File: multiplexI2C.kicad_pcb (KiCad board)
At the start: 2 copper layers, 48.3 x 71.1 mm, 58 parts, among them J1 Screw_Terminal_01x04, J10 Screw_Terminal_01x02, J2 Screw_Terminal_01x04, J3 Screw_Terminal_01x04, J4 Screw_Terminal_01x04, J5 Screw_Terminal_01x04, J6 Screw_Terminal_01x04, J7 Screw_Terminal_01x04, J8 Screw_Terminal_01x04, J9 Conn_02x04_Top_Bottom, U1 PCA9548A, U2 AMS1117-3.3 SOT-223, U3 f411-RFM95W

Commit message: cleaned up fab layer annotation.
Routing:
- net GND: track 69.9 -> 67.0 mm
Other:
- board text removed: "ADS1115IDGS"
- board text removed: "BT1"
- board text removed: "Battery_Cell_Holder"
- board text removed: "H1"
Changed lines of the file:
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@@
 		)
 		(property "Value" "1µF"
-			(at 1.33 0.19 90)
+			(at 2.9 0.22 90)
 			(layer "F.Fab")
 			(effects
@@
 		)
 		(property "Value" "MountingHole"
-			(at 1.34 4.23 0)
+			(at -3.76 6.2 45)
 			(layer "F.Fab")
 			(effects
@@
 		)
 		(property "Value" "TestPoint"
-			(at 0 1.55 0)
+			(at 3.87 -2.39 45)
 			(layer "F.Fab")
 			(effects
@@
 		(tags "SOT TO_SOT_SMD")
 		(property "Reference" "D3"
-			(at 0 -2.4 180)
+			(at 0.75 2.31 180)
 			(layer "F.SilkS")
 			(effects
@@
 		)
 		(property "Value" "BAT54C-HF"
-			(at -3.29 0.05 180)
+			(at -4.63 2.54 225)
 			(layer "F.Fab")
 			(effects
@@
 		)
 		(property "Value" "100nF"
-			(at 2.09 -0.09 90)
+			(at 3.25 0 90)
 			(layer "F.Fab")
 			(effects
@@
 		)
 		(property "Value" "Screw_Terminal_01x04"
-			(at 20.25 3.5 0)
+			(at 16.61 -6.03 45)
 			(layer "F.Fab")
 			(effects
@@
 		)
 		(property "Value" "0.1µF"
-			(at 0 1.16 0)
+			(at -0.06 -1.32 0)
 			(layer "F.Fab")
 			(effects
@@
 		)
 		(property "Value" "100nF"
-			(at 2.08 -0.05 90)
+			(at 3.37 0.2 90)
 			(layer "F.Fab")
 			(effects
@@
 		)
 		(property "Value" "MountingHole"
-			(at -7.67 -1.46 0)
+			(at 3.4 -6.43 45)
 			(layer "F.Fab")
 			(effects
@@
 		)
 		(property "Value" "100nF"
-			(at 2.11 -0.06 90)
+			(at 3.33 -0.07 90)
 			(layer "F.Fab")
 			(effects
@@
 		)
 		(property "Value" "MountingHole"
-			(at -1.12 3.57 0)
+			(at -3.27 5.84 45)
 			(layer "F.Fab")
 			(effects
@@
 		)
 		(property "Value" "Screw_Terminal_01x04"
-			(at -8.973 11.9275 0)
+			(at 17.127 -4.8825 45)
 			(layer "F.Fab")
 			(effects
@@
 		)
 		(property "Value" "AMS1117-3.3 SOT-223"
-			(at 0 4.5 0)
+			(at 6.81 -11.2 45)
 			(layer "F.Fab")
 			(effects
@@
 		)
 		(property "Value" "PCA9548A"
-			(at 0 4.85 0)
+			(at -4.5745 1.1075 45)
 			(layer "F.Fab")
 			(effects
@@
 		)
 		(property "Value" "f411-RFM95W"
-			(at -1.45 8.63 0)
+			(at 12.15 0.32 45)
 			(layer "F.Fab")
 			(effects
@@
 		)
 		(property "Value" "Screw_Terminal_01x02"
-			(at 1.016 12.192 90)
+			(at -4.73 10.33 45)
 			(layer "F.Fab")
 			(effects
@@
 		)
 		(property "Value" "100nF"
-			(at 0 0 90)
+			(at -3.3 0.03 90)
 			(layer "F.Fab")
 			(effects
@@
 		)
 		(property "Value" "MountingHole"
-			(at 1.629 -3.049 0)
+			(at 6.3 -5.77 45)
 			(layer "F.Fab")
 			(effects
@@
 		)
 		(property "Value" "0.1µF"
-			(at 0 0 180)
+			(at 0.36 1.21 180)
 			(layer "B.Fab")
 			(effects
@@
 		)
 		(property "Value" "4.7k"
-			(at 0 -0.1 90)
+			(at 2.04 1.4 90)
 			(layer "B.Fab")
 			(effects
@@
 		)
 		(property "Value" "100nF"
-			(at -0.22 -0.1 0)
+			(at -0.49 -1.11 0)
 			(layer "B.Fab")
 			(effects
@@
 		)
 		(property "Value" "0.1µF"
-			(at -0.75 0 0)
+			(at -0.39 1.32 0)
 			(layer "B.Fab")
 			(effects
@@
 			(at 0 7 180)
 			(layer "B.Fab")
+			(hide yes)
 			(effects
 				(font
@@
 		)
 		(property "Package" "BatteryHolder_LINX_BAT-HLD-012-SMT"
-			(at 0 0 180)
+			(at 13.87 7.61 315)
 			(unlocked yes)
 			(layer "B.Fab")
-			(hide yes)
 			(effects
 				(font
@@
 		)
 		(fp_text user "Pad  2 battery contact - no solder paste"
-			(at -0.29 -12.27 0)
+			(at 23.97 25.7 315)
 			(unlocked yes)
 			(layer "B.Fab")
@@
 		)
 		(property "Value" "4.7k"
-			(at -0.2 -0.15 90)
+			(at -0.95 -1.21 90)
 			(layer "B.Fab")
 			(effects
@@
 		)
 		(property "Value" "0.1µF"
-			(at 0 0 180)
+			(at 0.67 1.18 180)
 			(layer "B.Fab")
 			(effects
@@
 		)
 		(property "Value" "0.1µF"
-			(at 0 0 180)
+			(at 0.26 1.11 180)
 			(layer "B.Fab")
 			(effects
@@
 		)
 		(property "Value" "4.7k"
-			(at 0 0.1 90)
+			(at -1.28 -1.27 90)
 			(layer "B.Fab")
 			(effects
@@
 		)
 		(property "Value" "0.1µF"
-			(at 0 0 0)
+			(at 0.5 1.19 0)
 			(layer "B.Fab")
 			(effects
@@
 		)
 		(property "Value" "0.1µF"
-			(at 0 -1.16 0)
+			(at 0.6 1.05 0)
 			(layer "B.Fab")
 			(effects
@@
 		)
 		(property "Value" "0.1µF"
-			(at -0.38 -0.1 180)
+			(at 1.32 1.13 180)
 			(layer "B.Fab")
 			(effects
@@
 		)
 	)
-	(gr_text "Battery_Cell_Holder"
-		(at 87.609998 46.01 90)
-		(layer "B.Fab")
-		(effects
-			(font
-				(size 1 1)
-				(thickness 0.15)
-			)
-			(justify mirror)
-		)
-	)
-	(gr_text "BT1"
-		(at 87.619999 33.72 0)
-		(layer "B.Fab")
-		(effects
-			(font
-				(size 1 1)
-				(thickness 0.15)
-			)
-			(justify mirror)
-		)
-	)
-	(gr_text "ADS1115IDGS"
-		(at 73.84 56.02 90)
-		(layer "F.Fab")
-		(effects
-			(font
-				(size 1 1)
-				(thickness 0.15)
-			)
-		)
-	)
-	(gr_text "H1"
-		(at 96.29 95.15 0)
-		(layer "F.Fab")
-		(effects
-			(font
-				(size 1 1)
-				(thickness 0.15)
-			)
-		)
-	)
 	(gr_text "U2"
 		(at 72.84 57.02 270)
@@
 	)
 	(segment
-		(start 69.885 60.09)
-		(end 69.885 60.585)
-		(width 0.25)
-		(layer "B.Cu")
-		(net 2)
-	)
-	(segment
 		(start 64.94 51.65)
 		(end 64.9 51.69)
@@
 	)
 	(segment
-		(start 58.197 60.0775)
-		(end 58.197 60.617)
-		(width 0.25)
-		(layer "B.Cu")
-		(net 2)
-	)
-	(segment
 		(start 70.242 65.9025)
 		(end 70.917 65.2275)
@@
 	)
 	(segment
-		(start 69.84 40.92)
-		(end 69.84 40.44)
-		(width 0.25)
-		(layer "B.Cu")
-		(net 2)
-	)
-	(segment
 		(start 70.242 67.9075)
 		(end 70.242 65.9025)
@@
 	)
 	(segment
-		(start 58.214 33.415)
-		(end 58.214 33.924)
-		(width 0.25)
-		(layer "B.Cu")
-		(net 2)
-	)
-	(segment
 		(start 58.197 60.617)
 		(end 59.34 61.76)
@@
 	)
 	(segment
-		(start 58.182 67.9075)
-		(end 58.182 67.278)
-		(width 0.25)
-		(layer "B.Cu")
-		(net 2)
-	)
-	(segment
 		(start 65.64 51.65)
 		(end 64.94 51.65)
@@
 	)
 	(segment
-		(start 58.214 40.915)
-		(end 58.214 40.656)
-		(width 0.25)
-		(layer "B.Cu")
-		(net 2)
-	)
-	(segment
 		(start 59.07 32.559)
 		(end 58.214 33.415)
@@
 	)
 	(segment
-		(start 55.633 68.2545)
-		(end 55.633 67.9425)
-		(width 0.25)
-		(layer "F.Cu")
-		(net 38)
-	)
-	(segment
 		(start 51.189 56.520805)
 		(end 51.189 68.8905)
@@
 	)
 	(segment
-		(start 55.633 65.893)
-		(end 55.55 65.81)
-		(width 0.25)
-		(layer "B.Cu")
-		(net 38)
-	)
-	(segment
 		(start 52.646695 55.857805)
 		(end 51.639 56.8655)
@@
 		(width 0.25)
 		(layer "B.Cu")
-		(net 39)
-	)
-	(segment
-		(start 53.093 65.857)
-		(end 53.15 65.8)
-		(width 0.25)
-		(layer "B.Cu")

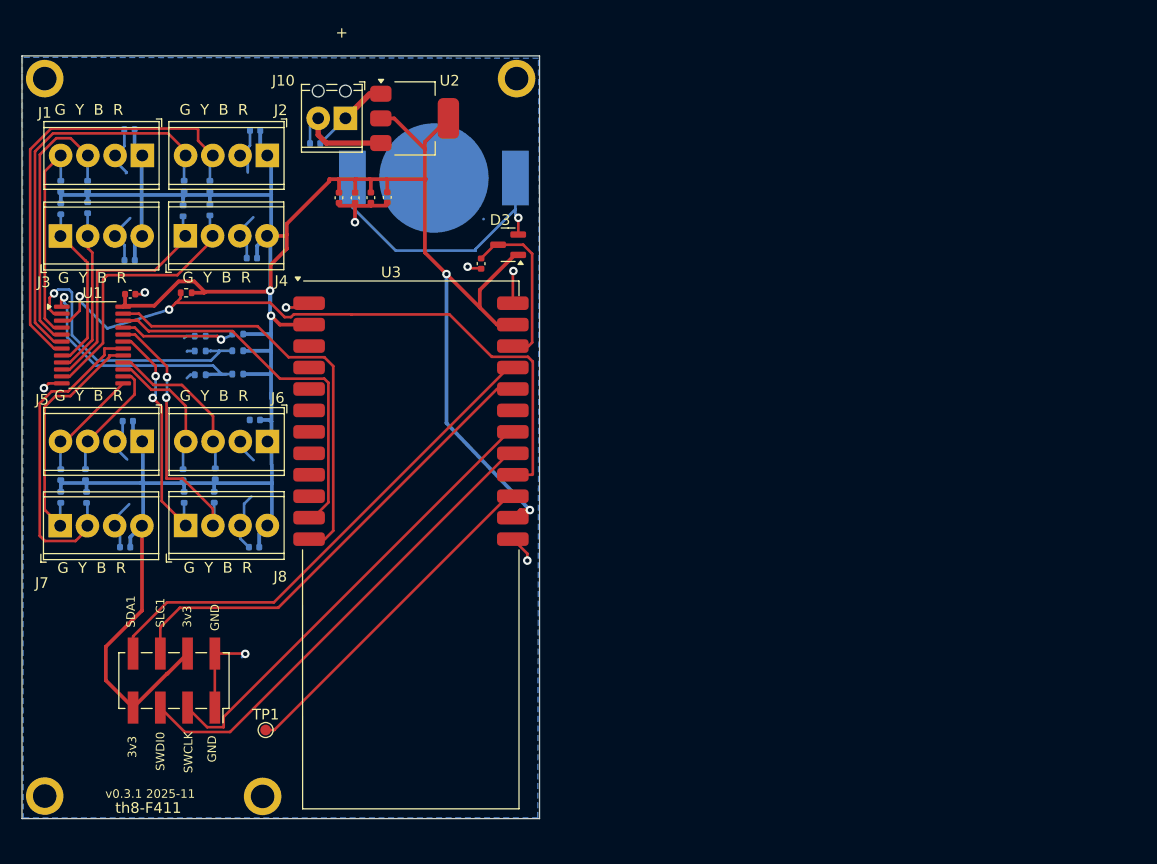
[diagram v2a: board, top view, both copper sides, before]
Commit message: schematic good. Footprint placement ongoing.
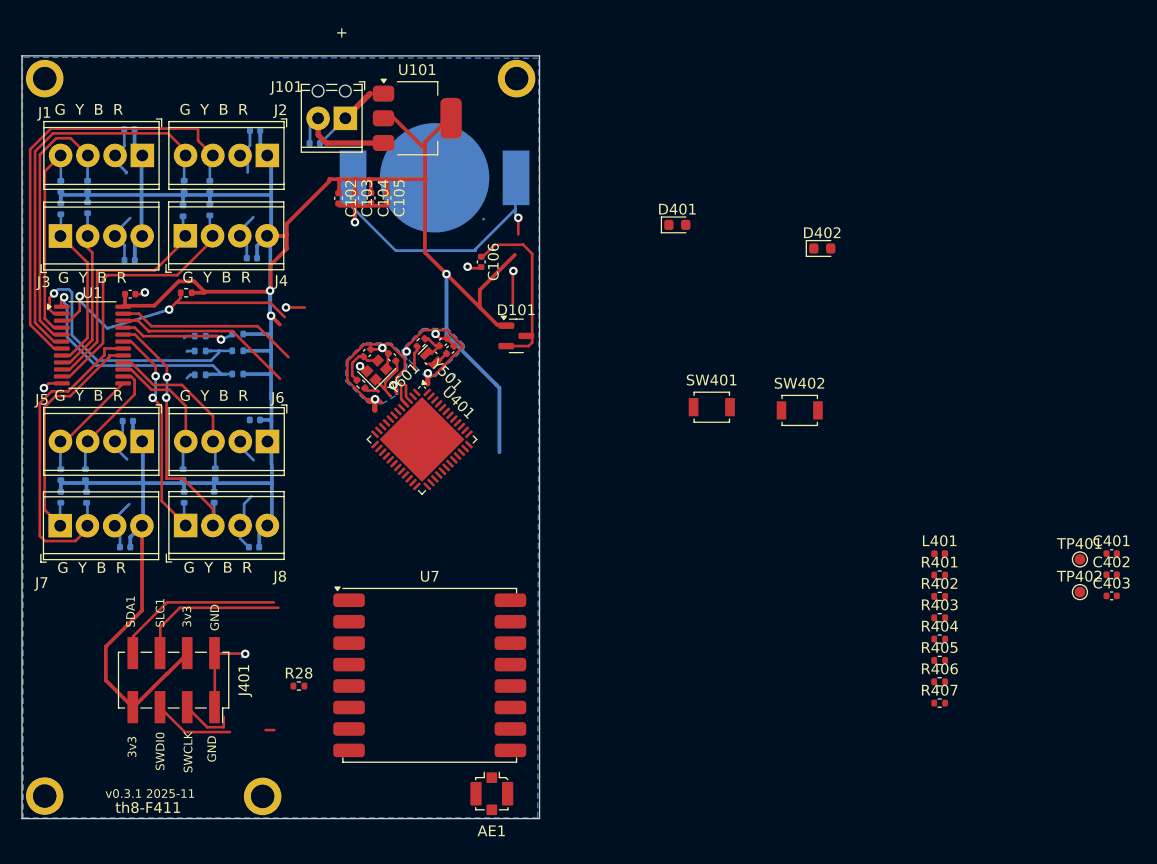
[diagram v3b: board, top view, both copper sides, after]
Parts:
- removed BT1: Battery_Cell_Holder, ProjectLib:BatteryHolder_LINX_BAT-HLD-012-SMT
- removed C10: 1µF, ProjectLib:C_0402_1005Metric
- removed C11, C12, C13, C14, C15: 100nF, ProjectLib:C_0402_1005Metric
- removed D3: BAT54C-HF, ProjectLib:SOT-23
- removed J10: Screw_Terminal_01x02, ProjectLib:TerminalBlock_Phoenix_MPT-0,5-2-2.54_1x02_P2.54mm_Horizontal
- removed J9: Conn_02x04_Top_Bottom, ProjectLib:PinSocket_2x04_P2.54mm_Vertical_SMD
- removed TP1: TestPoint, ProjectLib:TestPoint_Pad_D1.0mm
- removed U2: AMS1117-3.3 SOT-223, ProjectLib:SOT-223
- removed U3: f411-RFM95W, ProjectLib:Castellated_MCU-LoRa_20x50mm_2x12_P2.0mm_SMD
- added AE1: U.FL, ProjectLib:U.FL_Molex_MCRF_73412-0110_Vertical, F.Cu at (93.3, 92.9)
- added BT101: Battery_Cell_Holder, ProjectLib:BatteryHolder_LINX_BAT-HLD-012-SMT, B.Cu at (88.0, 35.5)
- added C101: 100nF, ProjectLib:C_0402_1005Metric, B.Cu at (76.8, 32.3)
- added C102: 1µF, ProjectLib:C_0402_1005Metric, F.Cu at (79.0, 37.4)
- added C103: 100nF, ProjectLib:C_0402_1005Metric, F.Cu at (80.5, 37.4)
- added C104: 100nF, ProjectLib:C_0402_1005Metric, F.Cu at (82.1, 37.4)
- added C105: 100nF, ProjectLib:C_0402_1005Metric, F.Cu at (83.6, 37.4)
- added C106: 100nF, ProjectLib:C_0402_1005Metric, F.Cu at (92.3, 43.3)
- added C401: 100nF, ProjectLib:C_0402_1005Metric, F.Cu at (151.1, 70.5)
- added C402: 100nF, ProjectLib:C_0402_1005Metric, F.Cu at (151.1, 72.5)
- added C403: 4.7µF, ProjectLib:C_0402_1005Metric, F.Cu at (151.1, 74.5)
- added C501: 4pF C0G, NP0, +/- 0.1pF, ProjectLib:C_0402_1005Metric, F.Cu at (88.8, 50.8)
- added C502: 4pF C0G, NP0, +/- 0.1pF, ProjectLib:C_0402_1005Metric, F.Cu at (89.5, 51.5)
- added C601: 10pF C0G, NP0, +/- 0.1pF, ProjectLib:C_0402_1005Metric, F.Cu at (81.7, 51.8)
- added C602: 10pF C0G, NP0, +/- 0.1pF, ProjectLib:C_0402_1005Metric, F.Cu at (84.0, 52.2)
- added D101: BAT54C-HF, ProjectLib:SOT-23, F.Cu at (95.6, 50.2)
- added D401: red 2ma 1.8Vf, ProjectLib:LED_0603_1608Metric, F.Cu at (110.6, 39.9)
- added D402: blue 2ma 2.65Vf, ProjectLib:LED_0603_1608Metric, F.Cu at (124.2, 42.1)
- added J101: Screw_Terminal_01x02, ProjectLib:TerminalBlock_Phoenix_MPT-0,5-2-2.54_1x02_P2.54mm_Horizontal, F.Cu at (79.7, 29.9)
- added J401: Conn_02x04_Top_Bottom, ProjectLib:PinSocket_2x04_P2.54mm_Vertical_SMD, F.Cu at (63.7, 82.3)
- added L401: 2.2uH, ProjectLib:L_0402_1005Metric, F.Cu at (135.1, 70.6)
- added NT501: NetTie_2, ProjectLib:NetTie-2_SMD_Pad0.5mm, F.Cu at (87.4, 54.2)
- added NT601: NetTie_2, ProjectLib:NetTie-2_SMD_Pad0.5mm, F.Cu at (82.4, 56.7)
- added R28: 10k 1%, ProjectLib:R_0402_1005Metric, F.Cu at (75.3, 82.9)
- added R401: 10k 1%, ProjectLib:R_0402_1005Metric, F.Cu at (135.1, 72.5)
- added R402: 10k 1%, ProjectLib:R_0402_1005Metric, F.Cu at (135.1, 74.5)
- added R403: 715 1%, ProjectLib:R_0402_1005Metric, F.Cu at (135.1, 76.5)
- added R404: 280 1%, ProjectLib:R_0402_1005Metric, F.Cu at (135.1, 78.5)
- added R405: 10k 1%, ProjectLib:R_0402_1005Metric, F.Cu at (135.1, 80.5)
- added R406: 10k 1%, ProjectLib:R_0402_1005Metric, F.Cu at (135.1, 82.5)
- added R407: 10k 1%, ProjectLib:R_0402_1005Metric, F.Cu at (135.1, 84.5)
- added R501: 0, ProjectLib:R_0402_1005Metric, F.Cu at (86.7, 50.9)
- added R601: 634 1%, ProjectLib:R_0402_1005Metric, F.Cu at (81.1, 54.7)
- added SW401: SW_Push, ProjectLib:SW_SPST_B3U-1000P, F.Cu at (113.8, 56.9)
- added SW402: SW_Push, ProjectLib:SW_SPST_B3U-1000P, F.Cu at (122.0, 57.2)
- added TP401: MCO, ProjectLib:TestPoint_Pad_D1.0mm, F.Cu at (148.2, 71.1)
- added TP402: BT1 b2, ProjectLib:TestPoint_Pad_D1.0mm, F.Cu at (148.2, 74.1)
- added U101: AMS1117-3.3 SOT-223, ProjectLib:SOT-223, F.Cu at (86.4, 29.9)
- added U401: STM32F411CEU6, ProjectLib:QFN-48-1EP_7x7mm_P0.5mm_EP5.6x5.6mm, F.Cu at (86.8, 59.9)
- added U7: RFM95W-915S2, ProjectLib:HOPERF_RFM9XW_SMD, F.Cu at (87.5, 81.9)
- added Y501: 32.758kHz, ProjectLib:Crystal_SMD_MicroCrystal_CM9V-T1A-2Pin_1.6x1.0mm, F.Cu at (87.7, 52.3)
- added Y601: 25MHz, ProjectLib:Crystal_SMD_2016-4Pin_2.0x1.6mm, F.Cu at (82.6, 53.4)
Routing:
- net /MCU-LoRa/SWDIO: track 44.2 -> 0.00 mm
- net /MCU-LoRa/SWCLK: track 42.7 -> 0.00 mm
- net PA9: track 63.6 -> 26.2 mm
- net Net-(U3-PA8-MCO): track 31.6 -> 0.00 mm
- net SDA1: track 47.0 -> 16.0 mm
- net SCL1: track 44.5 -> 14.2 mm
- net Net-(BT101-+): track 0.00 -> 26.7 mm, vias 0 -> 1
- net Net-(BT1-+): track 26.7 -> 0.00 mm, vias 1 -> 0
- net GND_HSE: track 0.00 -> 23.4 mm, vias 0 -> 4
- net SDA2: track 39.5 -> 17.1 mm
- net SCL2: track 36.1 -> 18.2 mm
- net GND_LSE: track 0.00 -> 14.5 mm, vias 0 -> 3
- net +3V3: track 257.8 -> 246.7 mm, vias 4 -> 3
- net /f411/SWDIO: track 0.00 -> 7.44 mm
- net GND: track 67.0 -> 61.5 mm, vias 8 -> 6
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- added copper zone on B.Cu, net GND_HSE
- added copper zone on B.Cu, net GND_LSE

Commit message: ongoing
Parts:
- removed C401: 100nF, ProjectLib:C_0402_1005Metric
- NT501, NT601: moved to B.Cu
- SW401: value SW_Push -> RST
- SW402: value SW_Push -> BT0
- moved R406 77.6 mm to (57.5, 82.4), turned to 90 degrees
- moved R407 73.5 mm to (62.3, 74.2), turned to 180 degrees
- moved C402 73.4 mm to (79.1, 58.2), turned to 180 degrees
- moved C403 68.3 mm to (83.5, 64.6), turned to 180 degrees
- moved R404 68.2 mm to (76.4, 43.7)
- moved R403 66.4 mm to (79.2, 40.8)
- moved TP402 65.0 mm to (83.7, 66.6)
- moved TP401 59.0 mm to (89.5, 65.9)
- moved L401 57.5 mm to (79.2, 57.2), turned to 180 degrees
- moved R405 52.9 mm to (83.5, 68.7), turned to -90 degrees
- moved D402 45.2 mm to (78.9, 43.8), turned to 180 degrees
- moved R401 43.5 mm to (91.6, 71.2)
- moved R402 43.2 mm to (92.5, 67.8)
- moved D401 34.1 mm to (76.6, 40.8), turned to 180 degrees
- moved SW402 29.6 mm to (93.7, 65.6), turned to 180 degrees
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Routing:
- net Net-(D402-K): track 0.00 -> 15.1 mm, vias 0 -> 2
- net +3V3: track 246.7 -> 254.6 mm
- net SCL1: track 14.2 -> 20.0 mm
- net Net-(U401-VDDA/VREF+): track 0.00 -> 5.14 mm
- net GND: track 61.5 -> 66.6 mm, vias 6 -> 8
- net PC14_OSC32_IN: track 3.00 -> 7.86 mm
- net NSS: track 0.00 -> 4.17 mm
- net PH1_OSC_OUT: track 1.40 -> 4.32 mm
- net PC15_OSC32_OUT: track 4.40 -> 7.11 mm
- net PH0_OSC_IN: track 5.30 -> 7.26 mm
- net GND_HSE: track 23.4 -> 21.7 mm
- net Net-(D401-K): track 0.00 -> 1.29 mm
- net Net-(D402-A): track 0.00 -> 1.24 mm
- net SDA1: track 16.0 -> 17.1 mm
- net (no net): track 0.80 -> 0.00 mm

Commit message: ERC and DRC good. Needs fab layer cleanup.
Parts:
- removed AE1: U.FL, ProjectLib:U.FL_Molex_MCRF_73412-0110_Vertical
- removed R28: 10k 1%, ProjectLib:R_0402_1005Metric
- removed U7: RFM95W-915S2, ProjectLib:HOPERF_RFM9XW_SMD
- added AE701: U.FL, ProjectLib:U.FL_Molex_MCRF_73412-0110_Vertical, F.Cu at (90.5, 90.5)
- added C401: 100nF, ProjectLib:C_0402_1005Metric, F.Cu at (75.3, 41.2)
- added G***: LOGO, ProjectLib:IDblock, F.Cu at (55.8, 75.9)
- added G1: LOGO, ProjectLib:SensorProject_QR, F.Cu at (68.2, 81.9)
- added G2: LOGO, ProjectLib:SensorProject_IDblock, F.Cu at (57.1, 80.0)
- added R408: 10k 1%, ProjectLib:R_0402_1005Metric, F.Cu at (72.0, 53.2)
- added R409: 10k 1%, ProjectLib:R_0402_1005Metric, F.Cu at (71.3, 48.7)
- added R701: 10k 1%, ProjectLib:R_0402_1005Metric, F.Cu at (77.7, 54.4)
- added U701: RFM95W-915S2, ProjectLib:HOPERF_RFM9XW_SMD, F.Cu at (86.0, 79.6)
- C101: moved to F.Cu
- R1, R2, R3, R4, R5, R6: value 0 -> 0k
- TP402: value BT1 b2 -> BT1
- moved SW401 33.3 mm to (77.1, 38.6)
- moved R401 32.5 mm to (79.8, 40.9), turned to 180 degrees
- moved R406 31.1 mm to (86.2, 70.6), turned to 180 degrees
- moved J401 30.5 mm to (88.3, 64.5), turned to 0 degrees
- moved SW402 29.1 mm to (82.8, 38.6), turned to 0 degrees
- moved R407 26.9 mm to (89.0, 70.6), turned to 0 degrees
- moved H1 23.7 mm to (95.7, 93.1)
- moved R402 19.2 mm to (90.6, 48.7), turned to -90 degrees
- moved D401 17.0 mm to (93.5, 39.6), turned to 90 degrees
- moved R404 15.6 mm to (92.0, 42.2), turned to 90 degrees
- moved D101 15.4 mm to (87.6, 37.1), turned to 90 degrees
- moved R403 14.0 mm to (93.1, 42.2), turned to -90 degrees
- moved D402 12.8 mm to (91.2, 40.4), turned to 0 degrees
- moved TP401 10.4 mm to (79.9, 61.9)
- moved TP402 10.3 mm to (79.9, 57.0)
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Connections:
- C501 pad 2: Net-(C13-Pad2) -> PC14_OSC32_IN
- C502 pad 2: PC14_OSC32_IN -> Net-(C502-Pad2)
- C601 pad 2: Net-(C10-Pad2) -> PH0_OSC_IN
- C602 pad 2: PH0_OSC_IN -> Net-(C602-Pad2)
- R501 pad 2: Net-(C13-Pad2) -> Net-(C502-Pad2)
- R601 pad 2: Net-(C10-Pad2) -> Net-(C602-Pad2)
- Y501 pad 1: Net-(C13-Pad2) -> Net-(C502-Pad2)
- Y601 pad 3: Net-(C10-Pad2) -> Net-(C602-Pad2)
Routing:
- net GND: track 66.6 -> 126.5 mm, vias 8 -> 15
- net +3V3: track 254.6 -> 295.7 mm, vias 3 -> 8
- net RESET: track 0.00 -> 36.6 mm
- net DIO0: track 0.00 -> 33.1 mm, vias 0 -> 2
- net DIO1: track 0.00 -> 31.6 mm, vias 0 -> 2
- net SCK: track 0.00 -> 27.6 mm
- net NSS: track 4.17 -> 31.1 mm
- net MOSI: track 0.00 -> 25.6 mm, vias 0 -> 2
- net SDA1: track 17.1 -> 41.9 mm, vias 0 -> 2
- net MISO: track 0.00 -> 23.8 mm
- net Net-(U401-NRST): track 0.00 -> 21.3 mm
- net SDA2: track 17.1 -> 37.8 mm, vias 0 -> 2
- net Net-(U401-BOOT0): track 0.00 -> 18.8 mm, vias 0 -> 2
- net PA9: track 26.2 -> 43.1 mm, vias 2 -> 4
- net SCL1: track 20.0 -> 36.9 mm, vias 0 -> 2
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- added copper zone on F.Cu, net GND_ANT
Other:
- board text added: "915MHz"
- board text added: "A"
- board text added: "HSE"
- board text added: "K"
- board text added: "LSE"
- board text added: "a8"
- board text added: "b2"
- board text added: "b8"
- board text added: "b9"
- board text added: "v0.3.1 2025-12"
- board text removed: "+"
- board text removed: "v0.3.1 2025-11"
